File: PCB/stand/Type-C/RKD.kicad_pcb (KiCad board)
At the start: 2 copper layers, 100 x 56.5 mm, 115 parts, among them J1 USB_C_Receptacle_USB2.0, J10 Conn_01x04_Male, J11 Conn_02x06_Odd_Even, J12 Conn_01x06, J13 Conn_01x03, J14 Conn_01x04, J15 Conn_01x04, J2 Conn_02x02_Odd_Even, J3 Conn_02x04_Odd_Even, J4 Conn_02x02_Odd_Even, J5 Conn_02x04_Odd_Even, K1 Key, K2 Key, K3 Key, K4 Key, SW2 SW_DIP_x04, SW3 SW_Push, SW5 SW_Push, U1 W25Q32JV, U2 RP2040, U3 CH9329, U4 AP1117-33, Y1 Crystal 12MHZ HC49, Y2 Crystal_GND24 12MHZ 3225

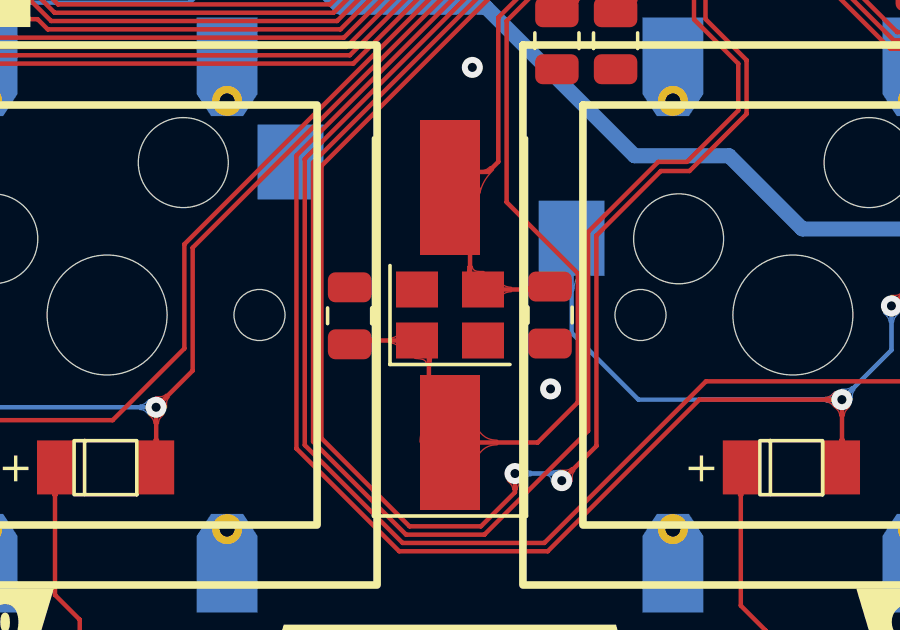
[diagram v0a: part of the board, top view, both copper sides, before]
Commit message: 紧急修复:经验证3225晶振无法稳定起振,故去除所以文件中的3225晶振
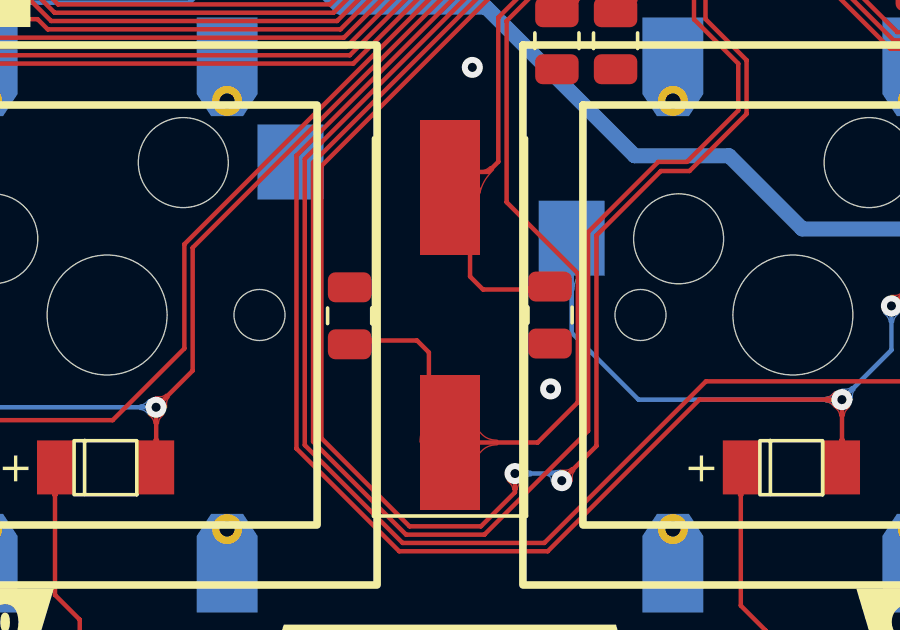
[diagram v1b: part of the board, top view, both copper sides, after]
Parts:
- removed Y2: Crystal_GND24 12MHZ 3225, Crystal:Crystal_SMD_3225-4Pin_3.2x2.5mm

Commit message: rename
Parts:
- removed kibuzzard-640C98B4: G***, kibuzzard-640C98B4
- added kibuzzard-64E6F25B: G***, kibuzzard-64E6F25B, B.Cu at (157.3, 85.1)
